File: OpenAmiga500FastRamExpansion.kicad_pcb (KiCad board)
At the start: 2 copper layers, 100 x 71.5 mm, 35 parts, among them J1 68000_SOCKET, P1 JTAG_CONNECTOR, P99 OSHW_LOGO, U1 68000D, U2 74LS157, U3 74LS157, U4 ATF1502AS-10JU44, U5 HYB5118160BSJ, U6 HYB5118160BSJ, U7 HYB5118160BSJ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

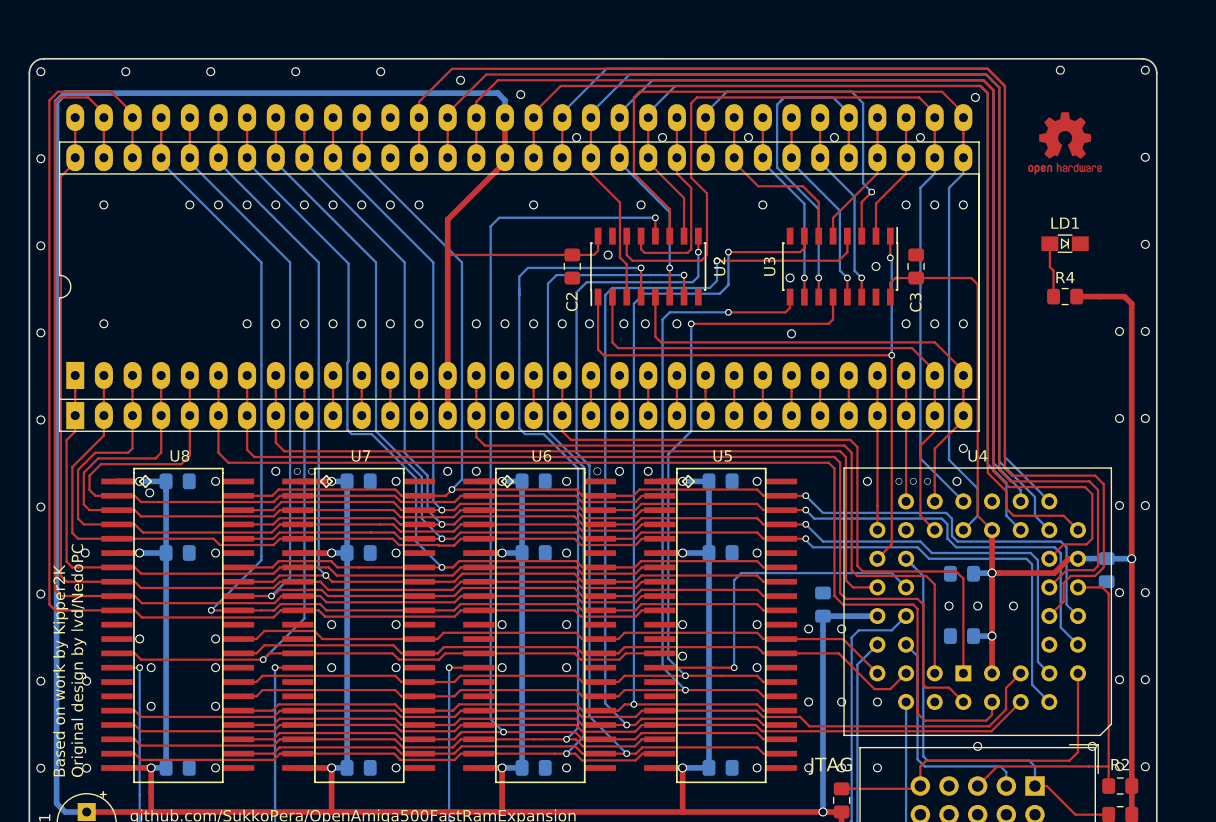
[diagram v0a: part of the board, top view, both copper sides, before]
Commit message: Autoconfig improvements * Add CFGIN * Add hardware to hide autoconfig cycles until configured   - Config before others   - No need for cfgout   - No need for cfgin if you want it to be the first dev configured
As of yet untested, waiting on parts and need to adapt code :)
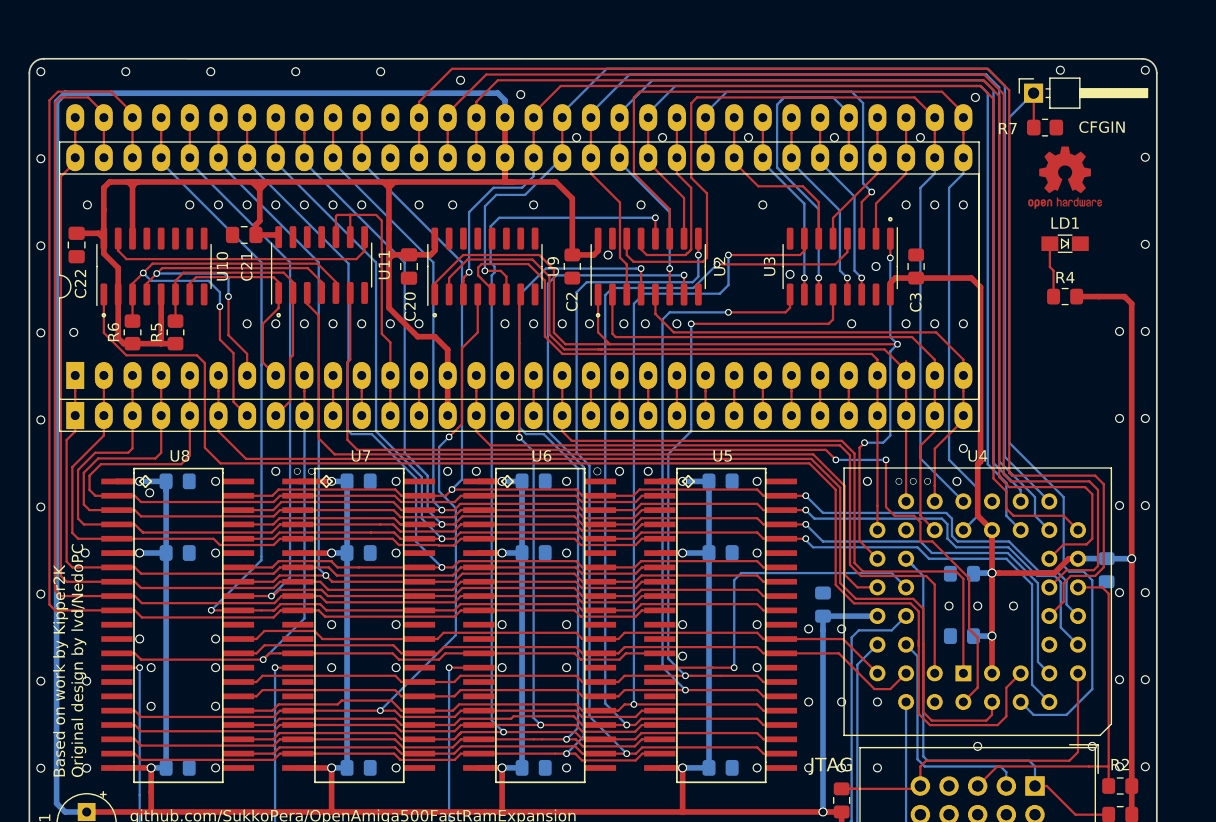
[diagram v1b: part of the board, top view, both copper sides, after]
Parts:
- added C20: 100n, Capacitor_SMD:C_0805_2012Metric_Pad1.18x1.45mm_HandSolder, F.Cu at (131.7, 68.8)
- added C21: 100n, Capacitor_SMD:C_0805_2012Metric_Pad1.18x1.45mm_HandSolder, F.Cu at (117.1, 66.0)
- added C22: 100n, Capacitor_SMD:C_0805_2012Metric_Pad1.18x1.45mm_HandSolder, F.Cu at (102.2, 66.9)
- added J2: CFGIN, Connector_PinHeader_2.54mm:PinHeader_1x01_P2.54mm_Horizontal, F.Cu at (187.1, 53.5)
- added R5: 4k7, Resistor_SMD:R_0805_2012Metric_Pad1.20x1.40mm_HandSolder, F.Cu at (111.0, 74.7)
- added R6: 4k7, Resistor_SMD:R_0805_2012Metric_Pad1.20x1.40mm_HandSolder, F.Cu at (107.2, 74.7)
- added R7: 10k, Resistor_SMD:R_0805_2012Metric_Pad1.20x1.40mm_HandSolder, F.Cu at (188.1, 56.5)
- added U10: 74LS257, Package_SO:SOIC-16_3.9x9.9mm_P1.27mm, F.Cu at (109.1, 68.8)
- added U11: 74HC00, Package_SO:SOIC-14_3.9x8.7mm_P1.27mm, F.Cu at (124.0, 68.7)
- added U9: 74LS157, Package_SO:SOIC-16_3.9x9.9mm_P1.27mm, F.Cu at (138.4, 68.8)
- moved P99 3.05 mm to (189.9, 61.0)
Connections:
- J1 pad 7: /~uds -> /~buds
- J1 pad 8: /~lds -> /~blds
- P1 pad 6: (no net) -> Net-(P1-Pad6)
- P1 pad 7: (no net) -> Net-(P1-Pad7)
- P1 pad 8: (no net) -> Net-(P1-Pad8)
- U1 pad 7: /~uds -> /~cpuuds
- U1 pad 8: /~lds -> /~cpulds
- U4 pad 33: /~lds -> /lds
- U4 pad 4: /ma1 -> /~cfgin
- U4 pad 44: /~uds -> /uds
- U4 pad 5: /ma0 -> /~cloak
- U5 pad 11: (no net) -> Net-(U5-Pad11)
- U5 pad 12: (no net) -> Net-(U5-Pad12)
- U5 pad 15: (no net) -> Net-(U5-Pad15)
- U5 pad 16: (no net) -> Net-(U5-Pad16)
- U5 pad 32: (no net) -> Net-(U5-Pad32)
- U6 pad 11: (no net) -> Net-(U6-Pad11)
- U6 pad 12: (no net) -> Net-(U6-Pad12)
- U6 pad 15: (no net) -> Net-(U6-Pad15)
- U6 pad 16: (no net) -> Net-(U6-Pad16)
- U6 pad 32: (no net) -> Net-(U6-Pad32)
- U7 pad 11: (no net) -> Net-(U7-Pad11)
- U7 pad 12: (no net) -> Net-(U7-Pad12)
- U7 pad 15: (no net) -> Net-(U7-Pad15)
- U7 pad 16: (no net) -> Net-(U7-Pad16)
- U7 pad 32: (no net) -> Net-(U7-Pad32)
- U8 pad 11: (no net) -> Net-(U8-Pad11)
- U8 pad 12: (no net) -> Net-(U8-Pad12)
- U8 pad 15: (no net) -> Net-(U8-Pad15)
- U8 pad 16: (no net) -> Net-(U8-Pad16)
- U8 pad 32: (no net) -> Net-(U8-Pad32)
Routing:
- net /~cloak: track 0.00 -> 117.6 mm
- net /~uds: track 90.3 -> 0.00 mm
- net VCC: track 550.7 -> 640.9 mm
- net /uds: track 0.00 -> 88.6 mm, vias 0 -> 2
- net /lds: track 0.00 -> 72.9 mm
- net /~lds: track 71.0 -> 0.00 mm
- net /~cfgin: track 0.00 -> 68.5 mm
- net /a2: track 11.2 -> 62.7 mm
- net /a1: track 13.7 -> 60.9 mm
- net /~cpuuds: track 0.00 -> 43.3 mm, vias 0 -> 2
- net /~buds: track 0.00 -> 34.4 mm, vias 0 -> 2
- net /~cpulds: track 0.00 -> 27.1 mm
- net /mux_switch: track 60.1 -> 86.1 mm, vias 2 -> 3
- net /DMA: track 0.00 -> 24.7 mm
- net /~bgack: track 3.56 -> 26.1 mm
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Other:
- board text added: "V1.5"
- board text removed: "V1"

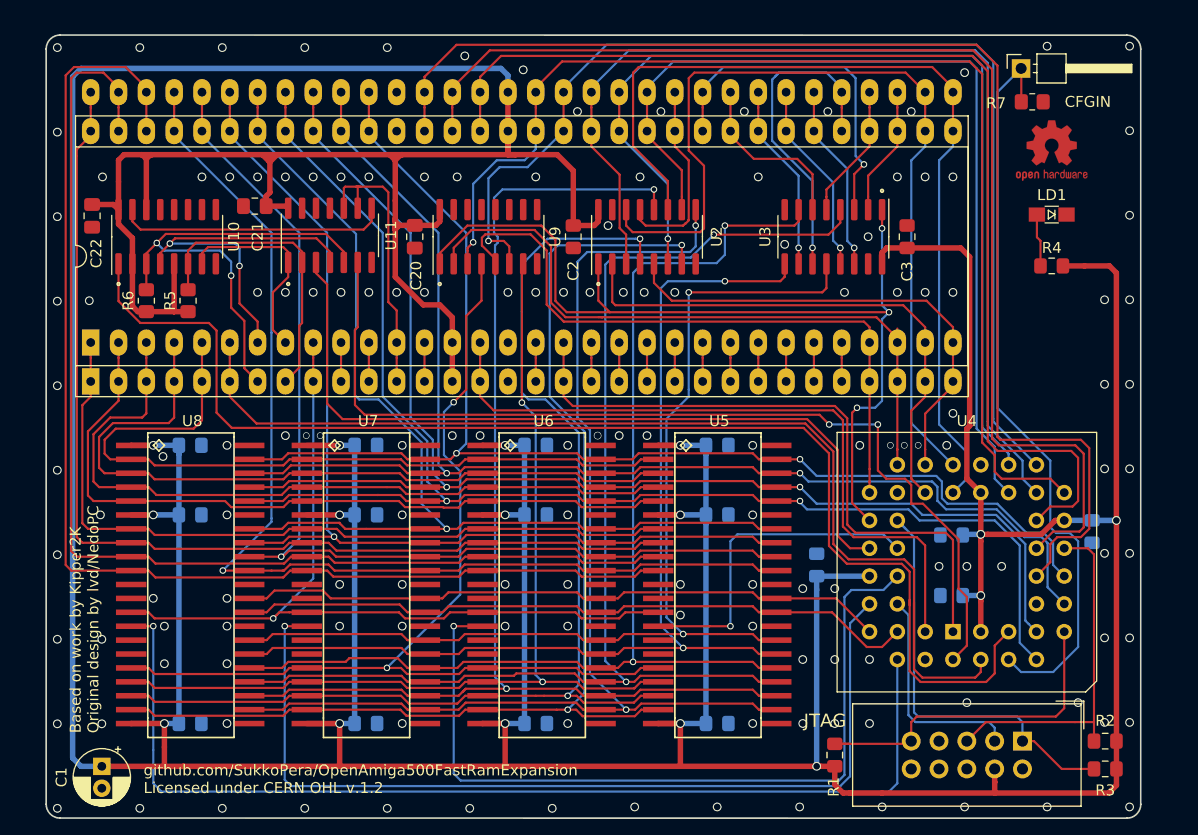
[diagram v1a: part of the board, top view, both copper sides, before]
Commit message: Isolate /AS too
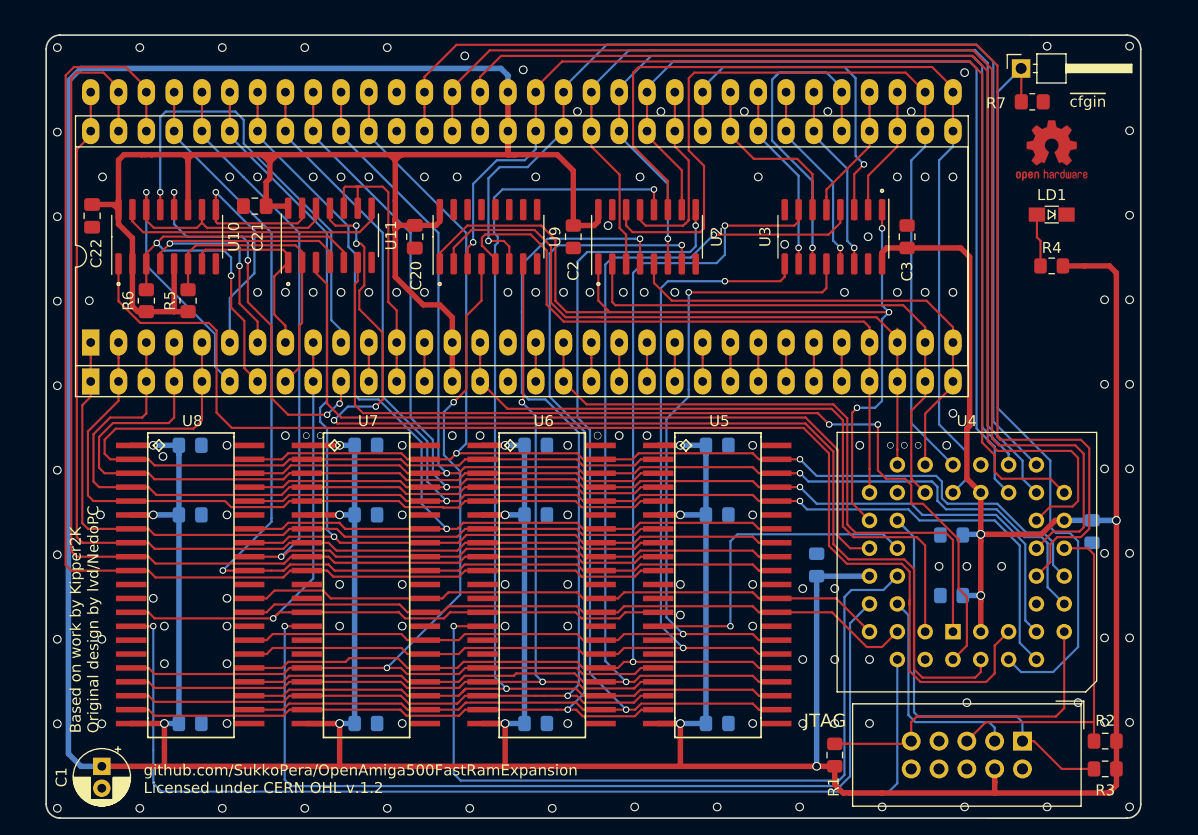
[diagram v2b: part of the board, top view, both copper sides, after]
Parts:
- J2: value CFGIN -> ~cfgin
- U10: value 74LS257 -> 74AHCT257
- U11: value 74HC00 -> 74AHC00
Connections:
- J1 pad 10: /~dtack -> /~bdtack
- J1 pad 6: /~as -> /~bas
- U1 pad 10: /~dtack -> /~cpudtack
- U1 pad 6: /~as -> /~cpuas
- U10 pad 10: VCC -> /~cpuas
- U10 pad 12: Net-(U10-Pad12) -> /~cpudtack
- U10 pad 13: VCC -> /~bdtack
- U10 pad 14: VCC -> /~cpuas
- U10 pad 9: Net-(U10-Pad9) -> /~bas
- U11 pad 11: Net-(U11-Pad11) -> /as
- U11 pad 12: GND -> /~cpuas
- U11 pad 13: GND -> /~bas
- U4 pad 2: /~as -> /as
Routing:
- net /as: track 0.00 -> 112.1 mm, vias 0 -> 4
- net /~as: track 101.0 -> 0.00 mm
- net /~cpuas: track 0.00 -> 41.7 mm, vias 0 -> 1
- net /~bdtack: track 0.00 -> 40.6 mm, vias 0 -> 1
- net /~cpudtack: track 0.00 -> 37.3 mm, vias 0 -> 4
- net /~bas: track 0.00 -> 27.9 mm, vias 0 -> 1
- net /~dtack: track 3.56 -> 0.00 mm
- net /clk: track 64.8 -> 64.0 mm
- net /~reset: track 60.0 -> 59.2 mm
- net VCC: track 640.9 -> 641.7 mm
- net /ma2: track 107.5 -> 106.9 mm
- net /d10: track 94.2 -> 94.7 mm
- net GND: vias 150 -> 148

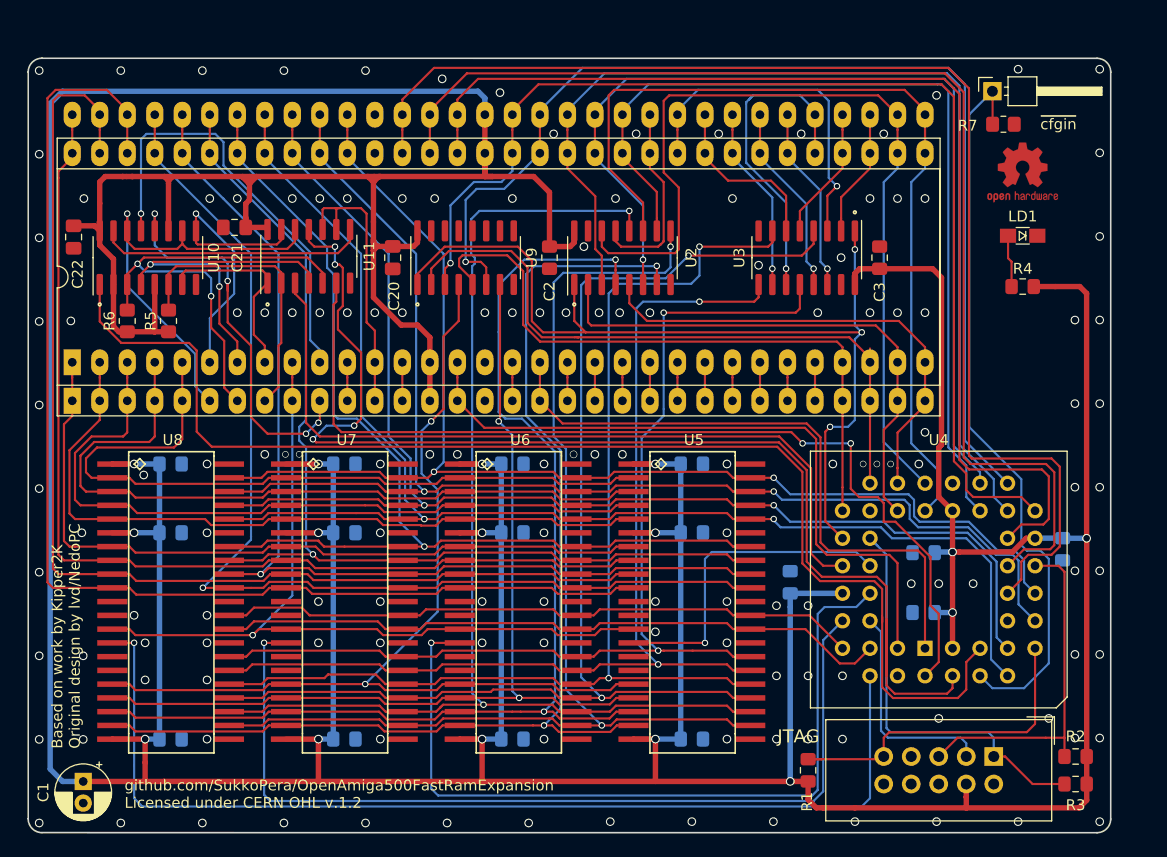
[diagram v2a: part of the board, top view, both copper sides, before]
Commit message: Add V2 Firmware, update documentation
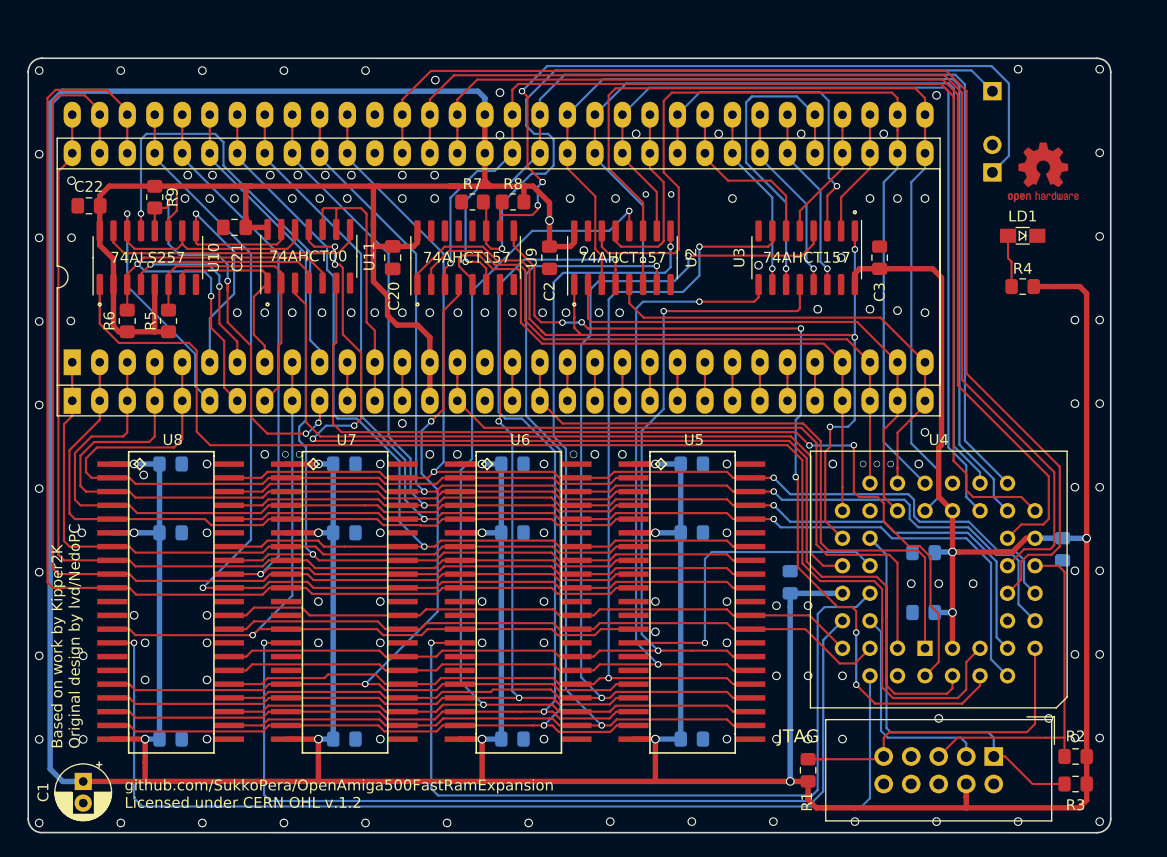
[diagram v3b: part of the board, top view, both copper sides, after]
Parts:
- added J3: 4MB, Connector_PinHeader_2.54mm:PinHeader_1x02_P2.54mm_Horizontal, B.Cu at (187.1, 61.0)
- added R8: 4k7, Resistor_SMD:R_0805_2012Metric_Pad1.20x1.40mm_HandSolder, F.Cu at (142.8, 63.7)
- added R9: 4k7, Resistor_SMD:R_0805_2012Metric_Pad1.20x1.40mm_HandSolder, F.Cu at (109.7, 63.2)
- J2: value ~cfgin -> cfgin; moved to B.Cu
- R7: value 10k -> 4k7
- U10: value 74AHCT257 -> 74ALS257
- U11: value 74AHC00 -> 74AHCT00
- U2, U3, U9: value 74LS157 -> 74AHCT157
- moved R7 49.5 mm to (139.1, 63.7), turned to 180 degrees
- moved C22 3.21 mm to (103.7, 64.0), turned to 180 degrees
- moved P99 1.91 mm to (191.8, 61.0)
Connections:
- J2 pad 1: /~cfgin -> Net-(J2-Pad1)
- R7 pad 1: /~cfgin -> Net-(J2-Pad1)
- U4 pad 4: /~cfgin -> /cfg
- U9 pad 10: GND -> Net-(J3-Pad1)
- U9 pad 11: GND -> Net-(J2-Pad1)
- U9 pad 9: Net-(U9-Pad9) -> /cfg
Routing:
- net /cfg: track 0.00 -> 83.8 mm, vias 0 -> 6
- net Net-(J3-Pad1): track 0.00 -> 73.7 mm, vias 0 -> 3
- net Net-(J2-Pad1): track 0.00 -> 69.7 mm, vias 0 -> 1
- net /~cfgin: track 68.5 -> 0.00 mm
- net VCC: track 641.7 -> 632.2 mm, vias 16 -> 17
- net /a23: track 116.9 -> 112.1 mm
- net /a21: track 103.8 -> 99.7 mm
- net /a22: track 109.9 -> 106.1 mm
- net /ma5: track 111.9 -> 108.5 mm
- net /~cpudtack: track 37.3 -> 39.5 mm
- net /a2: track 62.7 -> 60.8 mm
- net /a6: track 82.1 -> 83.3 mm
- net /a3: track 48.9 -> 47.9 mm
- net /a1: track 60.9 -> 59.9 mm
- net /mux_switch: track 86.1 -> 85.1 mm
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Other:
- board text added: "V2"
- board text removed: "V1.5"

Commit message: Fixup schematic + documentation
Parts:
- U4: value ATF1502AS-10JU44 -> ATF1504AS-10JU44

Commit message: Remove unnecessary via
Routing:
- net VCC: vias 17 -> 16
